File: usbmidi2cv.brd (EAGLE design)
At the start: 39 x 55.9 mm, 33 parts, among them IC1 LM324N

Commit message: melhorias na pcb
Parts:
- R5: device pot:B64W -> rcl:RTRIM3006P
- moved NOTE 9.25 mm to (45.7, 58.4)
- moved R5 5.24 mm to (49.5, 50.8)
- renumbered CONTROL_CHANGE to CTRL_CHANGE
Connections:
- net N$14: now also R5.2; no longer R5.S
- net N$18: now also R5.1; no longer R5.E
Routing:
- net N$18: track 8.89 -> 12.5 mm
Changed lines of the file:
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@@
 <grid distance="50" unitdist="mil" unit="mil" style="lines" multiple="1" display="no" altdistance="5" altunitdist="mil" altunit="mil"/>
 <layers>
-<layer number="1" name="Top" color="4" fill="1" visible="yes" active="yes"/>
+<layer number="1" name="Top" color="4" fill="1" visible="no" active="yes"/>
 <layer number="16" name="Bottom" color="1" fill="1" visible="yes" active="yes"/>
 <layer number="17" name="Pads" color="2" fill="1" visible="yes" active="yes"/>
@@
 <layer number="19" name="Unrouted" color="6" fill="1" visible="yes" active="yes"/>
 <layer number="20" name="Dimension" color="24" fill="1" visible="yes" active="yes"/>
-<layer number="21" name="tPlace" color="7" fill="1" visible="yes" active="yes"/>
+<layer number="21" name="tPlace" color="7" fill="1" visible="no" active="yes"/>
 <layer number="22" name="bPlace" color="7" fill="1" visible="yes" active="yes"/>
-<layer number="23" name="tOrigins" color="15" fill="1" visible="yes" active="yes"/>
+<layer number="23" name="tOrigins" color="15" fill="1" visible="no" active="yes"/>
 <layer number="24" name="bOrigins" color="15" fill="1" visible="no" active="yes"/>
-<layer number="25" name="tNames" color="7" fill="1" visible="yes" active="yes"/>
+<layer number="25" name="tNames" color="7" fill="1" visible="no" active="yes"/>
 <layer number="26" name="bNames" color="7" fill="1" visible="yes" active="yes"/>
-<layer number="27" name="tValues" color="7" fill="1" visible="yes" active="yes"/>
+<layer number="27" name="tValues" color="7" fill="1" visible="no" active="yes"/>
 <layer number="28" name="bValues" color="7" fill="1" visible="no" active="yes"/>
 <layer number="29" name="tStop" color="7" fill="3" visible="no" active="yes"/>
@@
 <attribute name="VALUE" x="21.59" y="44.704" size="0.0254" layer="27"/>
 </element>
-<element name="CONTROL_CHANGE" library="solpad" library_urn="urn:adsk.eagle:library:364" package="LSP10" package3d_urn="urn:adsk.eagle:package:26501/1" value="LSP10" x="43.18" y="48.26" smashed="yes">
+<element name="CTRL_CHANGE" library="solpad" library_urn="urn:adsk.eagle:library:364" package="LSP10" package3d_urn="urn:adsk.eagle:package:26501/1" value="LSP10" x="43.18" y="48.26" smashed="yes">
 <attribute name="NAME" x="41.91" y="45.72" size="1.27" layer="25" ratio="10"/>
 <attribute name="POPULARITY" value="52" x="83.82" y="27.94" size="1.778" layer="27" display="off"/>
@@
 <attribute name="VALUE" x="34.925" y="36.449" size="1.27" layer="27" ratio="10" rot="R90"/>
 </element>
-<element name="NOTE" library="solpad" library_urn="urn:adsk.eagle:library:364" package="LSP10" package3d_urn="urn:adsk.eagle:package:26501/1" value="LSP10" x="48.26" y="49.53" smashed="yes">
-<attribute name="NAME" x="49.53" y="48.26" size="1.27" layer="25" ratio="10"/>
-<attribute name="POPULARITY" value="52" x="83.82" y="16.51" size="1.778" layer="27" display="off"/>
-<attribute name="VALUE" x="48.26" y="49.784" size="0.0254" layer="27"/>
+<element name="NOTE" library="solpad" library_urn="urn:adsk.eagle:library:364" package="LSP10" package3d_urn="urn:adsk.eagle:package:26501/1" value="LSP10" x="45.72" y="58.42" smashed="yes">
+<attribute name="NAME" x="46.99" y="57.15" size="1.27" layer="25" ratio="10"/>
+<attribute name="POPULARITY" value="52" x="81.28" y="25.4" size="1.778" layer="27" display="off"/>
+<attribute name="VALUE" x="45.72" y="58.674" size="0.0254" layer="27"/>
 </element>
 <element name="PITCH_BEND" library="solpad" library_urn="urn:adsk.eagle:library:364" package="LSP10" package3d_urn="urn:adsk.eagle:package:26501/1" value="LSP10" x="27.94" y="31.75" smashed="yes">
@@
 <attribute name="VALUE" x="33.9344" y="55.3974" size="0.9906" layer="27" ratio="10"/>
 </element>
-<element name="R5" library="pot" library_urn="urn:adsk.eagle:library:331" package="B64W" package3d_urn="urn:adsk.eagle:package:22686/1" value="2k" x="50.8" y="55.88" smashed="yes" rot="R270">
-<attribute name="POPULARITY" value="0" x="44.45" y="17.78" size="1.778" layer="27" rot="R270" display="off"/>
-<attribute name="VALUE" x="52.197" y="56.515" size="1.27" layer="27" ratio="10" rot="R270"/>
+<element name="R5" library="rcl" library_urn="urn:adsk.eagle:library:334" package="RTRIM3006P" package3d_urn="urn:adsk.eagle:package:23758/1" value="2k" x="49.53" y="50.8" smashed="yes" rot="R270">
+<attribute name="POPULARITY" value="3" x="43.18" y="12.7" size="1.778" layer="27" rot="R270" display="off"/>
+<attribute name="SPICEMODEL" value="X" x="49.53" y="50.8" size="1.778" layer="27" rot="R270" display="off"/>
+<attribute name="SPICEPREFIXL" value="POT" x="49.53" y="50.8" size="1.778" layer="27" rot="R270" display="off"/>
+<attribute name="VALUE" x="50.927" y="51.435" size="1.27" layer="27" ratio="10" rot="R270"/>
 </element>
 <element name="R6" library="rcl" library_urn="urn:adsk.eagle:library:334" package="0207/12" package3d_urn="urn:adsk.eagle:package:23489/1" value="6k8" x="35.56" y="58.42" smashed="yes">
@@
 <via x="26.67" y="40.64" extent="1-16" drill="0.35"/>
 <wire x1="31.75" y1="40.64" x2="26.67" y2="40.64" width="1.6" layer="16"/>
-<via x="26.67" y="49.53" extent="1-16" drill="0.35" diameter="1.5"/>
-<via x="26.67" y="40.64" extent="1-16" drill="0.35" diameter="1.5"/>
+<via x="26.67" y="49.53" extent="1-16" drill="0.508" diameter="2.159"/>
+<via x="26.67" y="40.64" extent="1-16" drill="0.508" diameter="2.159"/>
 <wire x1="21.59" y1="58.42" x2="24.13" y2="58.42" width="1.6" layer="16"/>
 <wire x1="24.13" y1="58.42" x2="26.67" y2="55.88" width="1.6" layer="16"/>
@@
 <signal name="N$13">
 <contactref element="IC1" pad="14"/>
-<contactref element="CONTROL_CHANGE" pad="MP"/>
+<contactref element="CTRL_CHANGE" pad="MP"/>
 <contactref element="IC1" pad="13"/>
 <wire x1="39.37" y1="50.8" x2="39.37" y2="48.26" width="1.6" layer="16"/>
@@
 <contactref element="IC1" pad="1"/>
 <contactref element="NOTE" pad="MP"/>
-<contactref element="R5" pad="S"/>
+<contactref element="R5" pad="2"/>
 <wire x1="31.75" y1="50.8" x2="31.75" y2="53.34" width="1.6" layer="16"/>
 <via x="31.75" y="53.34" extent="1-16" drill="0.35"/>
 <wire x1="31.75" y1="53.34" x2="45.72" y2="53.34" width="1.6" layer="1"/>
 <via x="45.72" y="53.34" extent="1-16" drill="0.35"/>
-<wire x1="45.72" y1="53.34" x2="48.26" y2="55.88" width="1.6" layer="16"/>
-<wire x1="48.26" y1="55.88" x2="48.26" y2="49.53" width="1.6" layer="16"/>
-<via x="31.75" y="53.34" extent="1-16" drill="0.35" diameter="1.5"/>
-<via x="45.72" y="53.34" extent="1-16" drill="0.35" diameter="1.5"/>
+<via x="31.75" y="53.34" extent="1-16" drill="0.508" diameter="2.159"/>
+<via x="45.72" y="53.34" extent="1-16" drill="0.508" diameter="2.159"/>
+<wire x1="45.72" y1="58.42" x2="45.72" y2="53.34" width="1.6" layer="16"/>
+<wire x1="45.72" y1="53.34" x2="48.26" y2="53.34" width="1.6" layer="16"/>
+<wire x1="48.26" y1="53.34" x2="48.26" y2="50.8" width="1.6" layer="16"/>
 </signal>
 <signal name="N$17">
@@
 <signal name="N$18">
 <contactref element="R6" pad="2"/>
-<contactref element="R5" pad="E"/>
-<wire x1="41.91" y1="58.42" x2="50.8" y2="58.42" width="1.6" layer="16"/>
+<contactref element="R5" pad="1"/>
+<wire x1="41.91" y1="58.42" x2="41.91" y2="59.69" width="1.6" layer="16"/>
+<wire x1="41.91" y1="59.69" x2="43.18" y2="60.96" width="1.6" layer="16"/>
+<wire x1="43.18" y1="60.96" x2="49.53" y2="60.96" width="1.6" layer="16"/>
+<wire x1="49.53" y1="60.96" x2="50.8" y2="59.69" width="1.6" layer="16"/>
+<wire x1="50.8" y1="59.69" x2="50.8" y2="58.42" width="1.6" layer="16"/>
 </signal>
 <signal name="N$19">

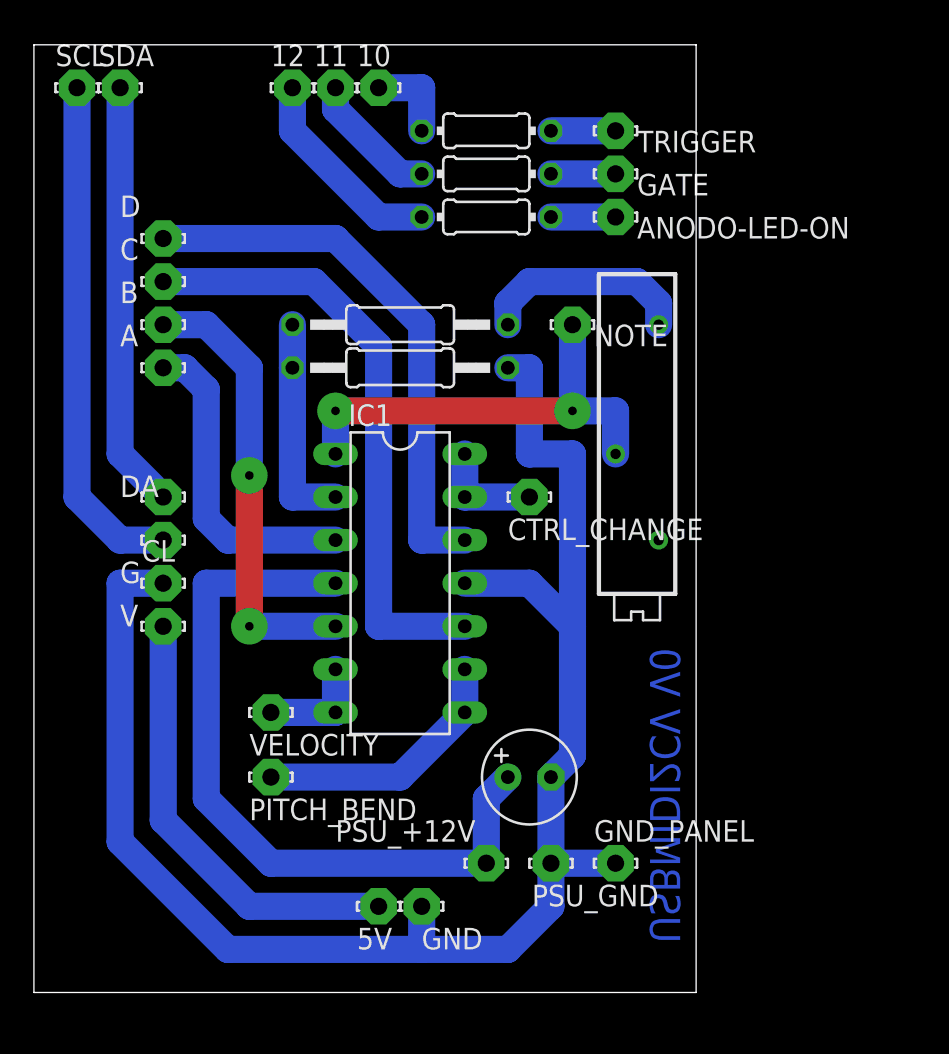
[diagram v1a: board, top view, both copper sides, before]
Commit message: change soldpad size
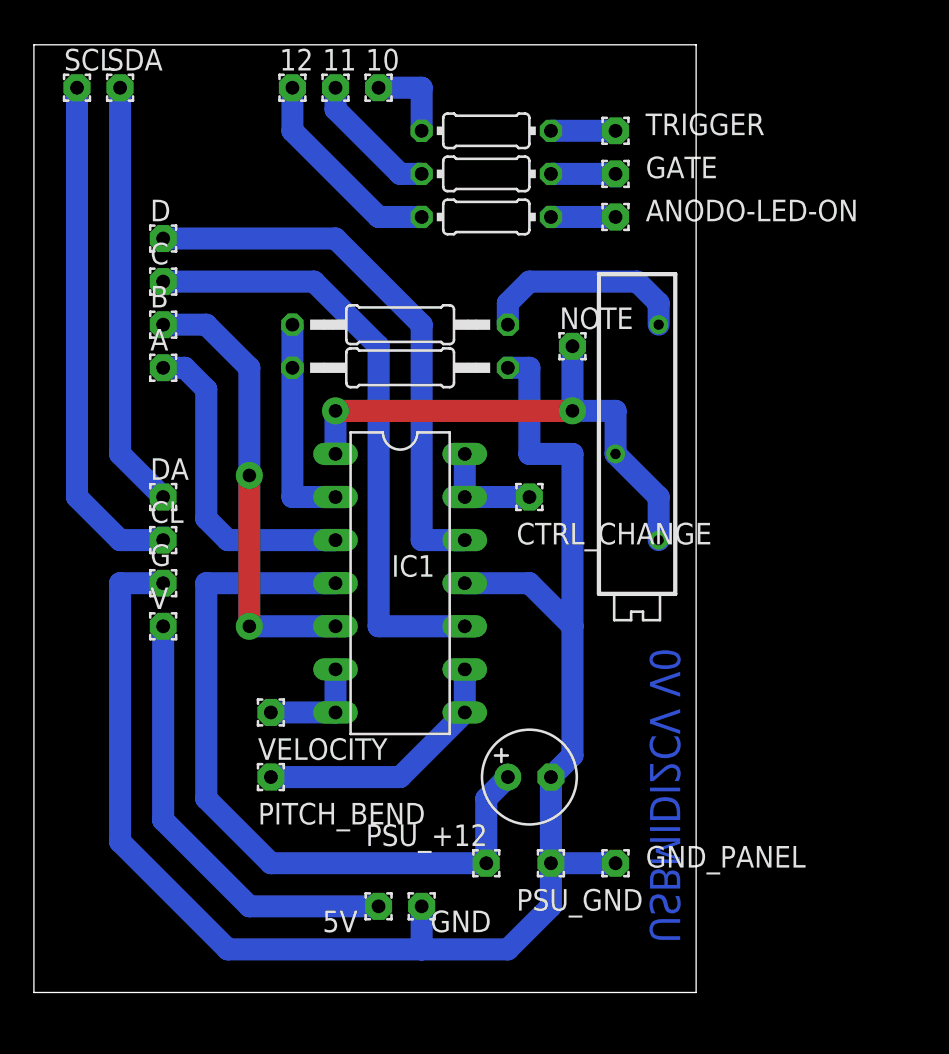
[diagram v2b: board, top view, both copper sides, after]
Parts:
- removed PSU_+12V: LSP10, solpad:LSP10
- added PSU_+12: (no value), wirepad:1,6/0,8
- 10, 11, 12, 5V, A, ANODO-LED-ON, B, C, CL, CTRL_CHANGE, D, DA, G, GATE, GND, GND_PANEL, NOTE, PITCH_BEND, PSU_GND, SCL, SDA, TRIGGER, V, VELOCITY: value LSP10 -> (none); device solpad:LSP10 -> wirepad:1,6/0,8
- moved NOTE 1.27 mm to (45.7, 57.1)
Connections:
- net GND: now also G.1, GND.1, GND_PANEL.1, PSU_GND.1; no longer G.MP, GND.MP, GND_PANEL.MP, PSU_GND.MP
- net N$1: now also A.1; no longer A.MP
- net N$10: now also DA.1, SDA.1; no longer DA.MP, SDA.MP
- net N$11: now also B.1; no longer B.MP
- net N$12: now also C.1; no longer C.MP
- net N$13: now also CTRL_CHANGE.1; no longer CTRL_CHANGE.MP
- net N$14: now also NOTE.1, R5.3; no longer NOTE.MP
- net N$15: now also PITCH_BEND.1; no longer PITCH_BEND.MP
- net N$16: now also VELOCITY.1; no longer VELOCITY.MP
- net N$19: now also PSU_+12.1; no longer PSU_+12V.MP
- net N$2: now also TRIGGER.1; no longer TRIGGER.MP
- net N$20: now also D.1; no longer D.MP
- net N$3: now also GATE.1; no longer GATE.MP
- net N$4: now also 10.1; no longer 10.MP
- net N$5: now also 11.1; no longer 11.MP
- net N$6: now also ANODO-LED-ON.1; no longer ANODO-LED-ON.MP
- net N$7: now also 12.1; no longer 12.MP
- net N$8: now also 5V.1, V.1; no longer 5V.MP, V.MP
- net N$9: now also CL.1, SCL.1; no longer CL.MP, SCL.MP
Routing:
- net N$14: track 26.7 -> 31.5 mm
